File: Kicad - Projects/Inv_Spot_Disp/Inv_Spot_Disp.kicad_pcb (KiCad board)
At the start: 2 copper layers, 137.8 x 68.7 mm, 44 parts, among them J1 PWM_Out, J2 Power_Supply, J3 Current_Sense, J4 Prog, SW1 1, SW2 2, SW3 3, SW4 4, SW5 SW_Push, U1 STM32F030F4Px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

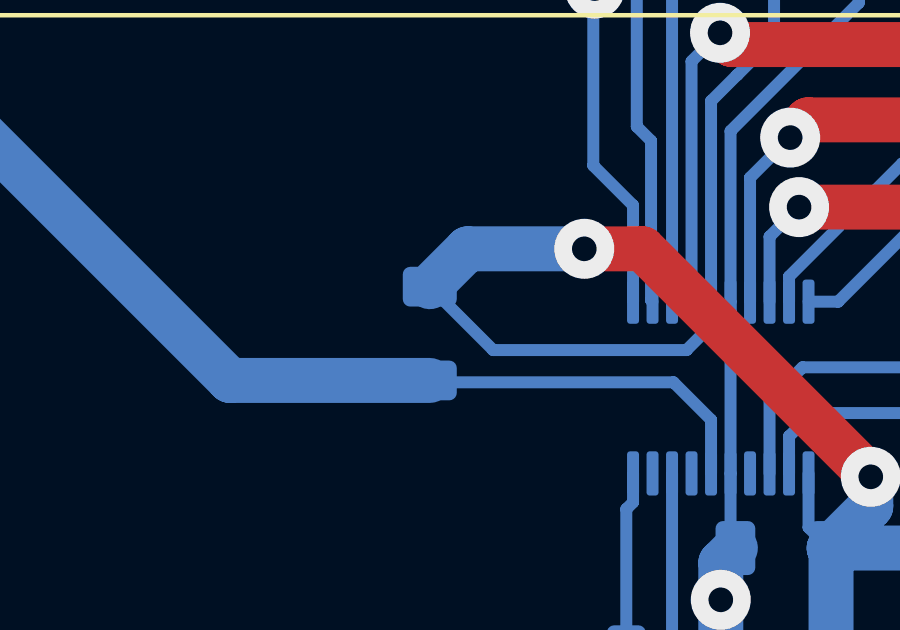
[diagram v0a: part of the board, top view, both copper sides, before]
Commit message: Ajustes de Documentação
Ajustada documentação do módulo LCD e corrigido erro de máscara na função HD_Set_Cursor

Ajustada também posição de capacitor de desacoplamento do sinal do sensor da corrente para ser mais próximo do ADC.
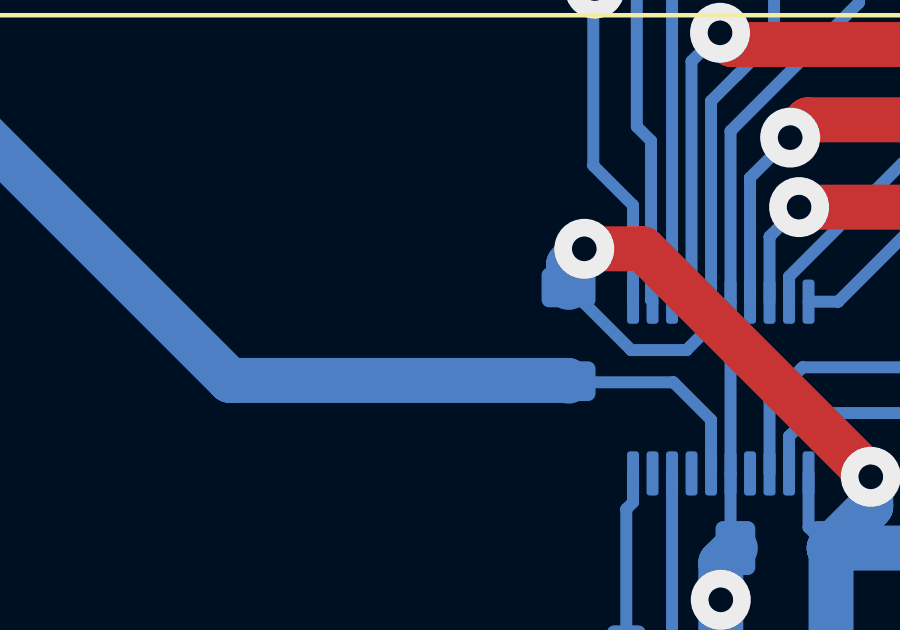
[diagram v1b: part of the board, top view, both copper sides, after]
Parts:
- moved C12 4.63 mm to (91.0, 84.3)
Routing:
- net GND: track 401.3 -> 392.5 mm
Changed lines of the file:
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@@
 	(footprint "Capacitor_SMD:C_1206_3216Metric_Pad1.33x1.80mm_HandSolder"
 		(layer "B.Cu")
-		(at 86.325 84.275 90)
+		(at 90.95 84.3 90)
 		(descr "Capacitor SMD 1206 (3216 Metric), square (rectangular) end terminal, IPC-7351 nominal with elongated pad for handsoldering. (Body size source: IPC-SM-782 page 76, https://www.pcb-3d.com/wordpress/wp-content/uploads/ipc-sm-782a_amendment_1_and_2.pdf)")
 		(tags "capacitor handsolder")
@@
 	)
 	(segment
-		(start 95.7 83.2125)
-		(end 95.7 84.009878)
-		(width 0.4)
-		(layer "B.Cu")
-		(net "GND")
-	)
-	(segment
 		(start 48.3125 76.9425)
 		(end 48.3125 89.8275)
@@
 	)
 	(segment
-		(start 91.475 81.45)
-		(end 87.5875 81.45)
-		(width 1.5)
-		(layer "B.Cu")
-		(net "GND")
-	)
-	(segment
 		(start 92.84 64.98)
 		(end 92.84 62.5)
@@
 	)
 	(segment
-		(start 95.7 84.009878)
-		(end 94.884878 84.825)
+		(start 94.884878 84.825)
+		(end 93.0375 84.825)
 		(width 0.4)
 		(layer "B.Cu")
@@
 	)
 	(segment
+		(start 95.7 83.2125)
+		(end 95.7 84.009878)
+		(width 0.4)
+		(layer "B.Cu")
+		(net "GND")
+	)
+	(segment
+		(start 90.95 81.975)
+		(end 90.95 82.7375)
+		(width 1.5)
+		(layer "B.Cu")
+		(net "GND")
+	)
+	(segment
 		(start 97.8 74.425)
 		(end 97.8 64.05)
@@
 	)
 	(segment
+		(start 95.7 84.009878)
+		(end 94.884878 84.825)
+		(width 0.4)
+		(layer "B.Cu")
+		(net "GND")
+	)
+	(segment
 		(start 128.24 58.64)
 		(end 131.55 61.95)
@@
 	)
 	(segment
-		(start 94.884878 84.825)
-		(end 88.4375 84.825)
-		(width 0.4)
-		(layer "B.Cu")
-		(net "GND")
-	)
-	(segment
 		(start 34.45 87.45)
 		(end 33.525 86.525)
@@
 	)
 	(segment
-		(start 80.192677 58.205177)
-		(end 81.1375 59.15)
+		(start 91.475 81.45)
+		(end 90.95 81.975)
 		(width 1.5)
 		(layer "B.Cu")
@@
 	)
 	(segment
-		(start 48.3125 76.9425)
-		(end 48.3125 83.4625)
+		(start 80.192677 58.205177)
+		(end 81.1375 59.15)
 		(width 1.5)
 		(layer "B.Cu")
@@
 	)
 	(segment
-		(start 87.5875 81.45)
-		(end 86.325 82.7125)
+		(start 48.3125 76.9425)
+		(end 48.3125 83.4625)
 		(width 1.5)
 		(layer "B.Cu")
@@
 	)
 	(segment
+		(start 93.0375 84.825)
+		(end 90.95 82.7375)
+		(width 0.4)
+		(layer "B.Cu")
+		(net "GND")
+	)
+	(segment
 		(start 95.7 76.525)
 		(end 96.575 75.65)
@@
 	)
 	(segment
-		(start 88.4375 84.825)
-		(end 86.325 82.7125)
-		(width 0.4)
-		(layer "B.Cu")
-		(net "GND")
-	)
-	(segment
 		(start 114.435 62.385)
 		(end 114.435 63.885)
@@
 	)
 	(segment
-		(start 94.45 85.9)
-		(end 86.3875 85.9)
+		(start 90.9875 85.9)
+		(end 90.95 85.8625)
 		(width 0.4)
 		(layer "B.Cu")
@@
 	)
 	(segment
-		(start 95.7 88.9375)
-		(end 95.7 87.15)
-		(width 0.4)
+		(start 65.575 71.75)
+		(end 79.6625 85.8375)
+		(width 1.5)
+		(layer "B.Cu")
+		(net "Current_Sense")
+	)
+	(segment
+		(start 79.6625 85.8375)
+		(end 90.925 85.8375)
+		(width 1.5)
 		(layer "B.Cu")
 		(net "Current_Sense")
@@
 	)
 	(segment
-		(start 65.575 71.75)
-		(end 79.6625 85.8375)
-		(width 1.5)
+		(start 95.7 88.9375)
+		(end 95.7 87.15)
+		(width 0.4)
 		(layer "B.Cu")
 		(net "Current_Sense")
 	)
 	(segment
-		(start 79.6625 85.8375)
-		(end 86.325 85.8375)
-		(width 1.5)
+		(start 94.45 85.9)
+		(end 90.9875 85.9)
+		(width 0.4)
 		(layer "B.Cu")
 		(net "Current_Sense")
 	)
 	(segment
-		(start 86.3875 85.9)
-		(end 86.325 85.8375)
-		(width 0.4)
+		(start 90.925 85.8375)
+		(end 90.95 85.8625)
+		(width 1.5)
 		(layer "B.Cu")
 		(net "Current_Sense")

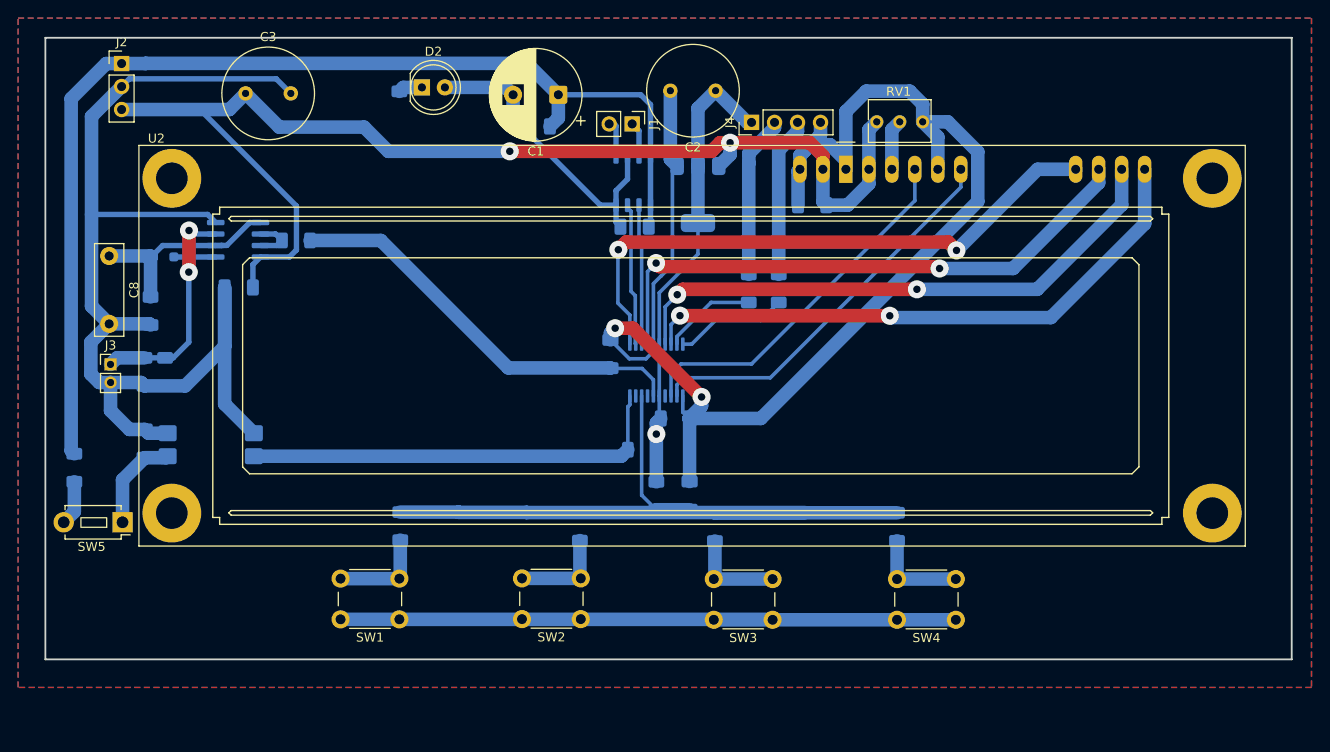
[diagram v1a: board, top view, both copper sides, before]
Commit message: Corrigido Footprint do Display
Corrigido problema com o footprint do display

Melhora o caminho de retorna das trilhas de programação

Aumento na quantidade de vias para reduzir impedância do plano terra
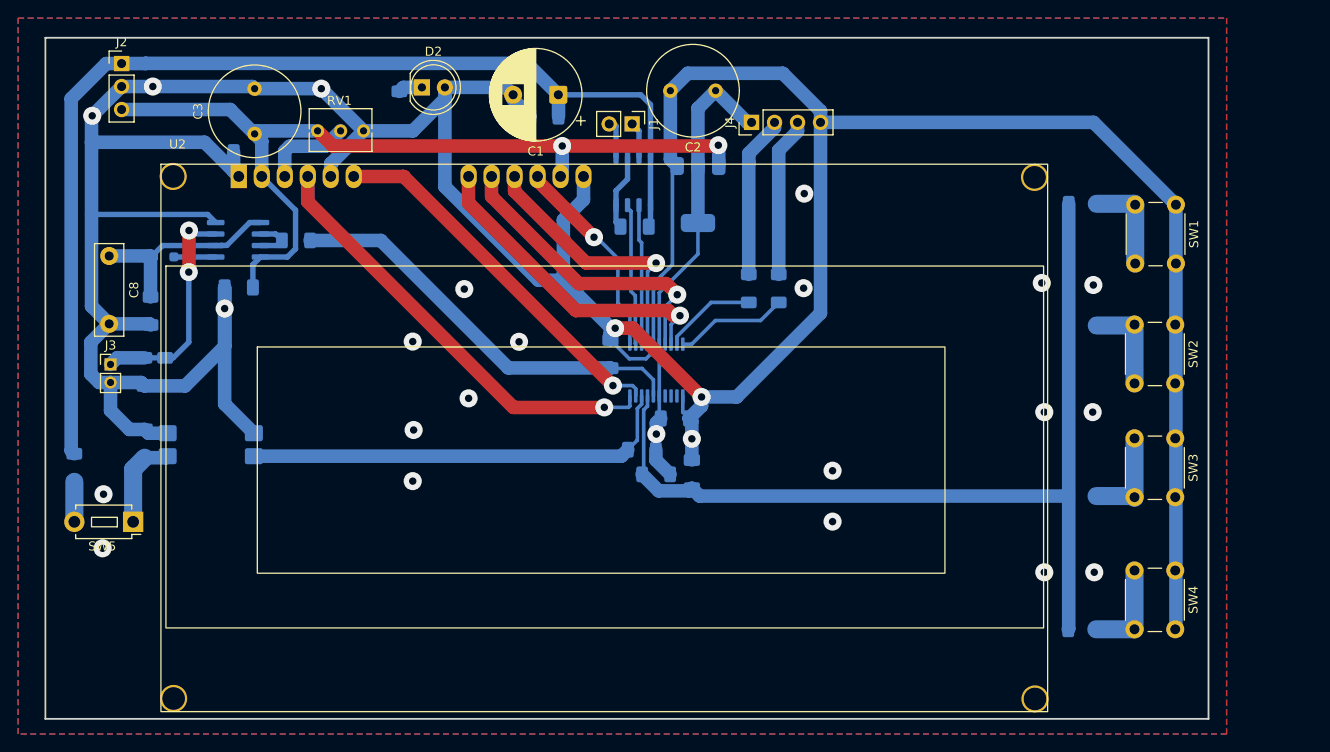
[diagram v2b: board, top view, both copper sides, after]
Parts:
- U2: value LCD-016N002L -> NHD-0420H1Z; footprint Display:LCD-016N002L -> Display:WC1602A
- moved SW1 97.3 mm to (153.4, 67.8), turned to -90 degrees
- moved R2 83.4 mm to (143.2, 67.7), turned to 0 degrees
- moved SW2 73.3 mm to (153.4, 81.0), turned to -90 degrees
- moved U2 67.1 mm to (49.9, 64.7)
- moved C5 62.6 mm to (50.9, 62.0)
- moved RV1 61.8 mm to (58.6, 59.6)
- moved R3 59.9 mm to (143.2, 81.2), turned to 0 degrees
- moved SW3 48.8 mm to (153.4, 93.6), turned to -90 degrees
- moved R4 40.8 mm to (143.1, 100.0), turned to 0 degrees
- moved SW4 24.9 mm to (153.4, 108.2), turned to -90 degrees
- moved R5 23.4 mm to (143.1, 114.7), turned to 0 degrees
- moved C3 4.59 mm to (51.6, 60.0), turned to 90 degrees
- moved C6 2.39 mm to (100.0, 97.6)
- moved R1 2.38 mm to (96.0, 97.6), turned to 180 degrees
- moved C10 1.45 mm to (83.7, 58.0)
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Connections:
- U1 pad 10: Trigger -> RS
- U1 pad 11: D4 -> D7
- U1 pad 14: D5 -> D6
- U1 pad 17: D6 -> D5
- U1 pad 18: D7 -> D4
- U1 pad 2: Enable -> unconnected-(U1-PF0-Pad2)
- U1 pad 3: RS -> unconnected-(U1-PF1-Pad3)
- U1 pad 7: Temp_Sense -> Display_ADC
- U1 pad 8: Display_ADC -> Trigger
- U1 pad 9: unconnected-(U1-PA3-Pad9) -> Enable
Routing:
- net GND: track 392.5 -> 451.2 mm, vias 2 -> 25
- net 5V: track 140.1 -> 96.2 mm
- net D7: track 65.3 -> 22.9 mm, vias 2 -> 1
- net D6: track 63.2 -> 29.9 mm, vias 2 -> 1
- net D4: track 66.0 -> 35.0 mm, vias 2 -> 1
- net D5: track 63.9 -> 33.3 mm, vias 2 -> 1
- net Display_ADC: track 81.9 -> 104.3 mm
- net RS: track 40.8 -> 49.0 mm, vias 0 -> 1
- net Net-(U2-VO): track 5.61 -> 9.90 mm
- net Enable: track 43.6 -> 41.7 mm, vias 0 -> 1
- net 3V3: track 51.5 -> 49.6 mm
- net 15V: track 124.4 -> 122.9 mm
- net Trigger: track 47.7 -> 48.2 mm
- net Net-(C9-Pad1): track 10.8 -> 10.2 mm
- net Net-(R8-Pad1): track 4.96 -> 4.42 mm
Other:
- board size 137.8 x 68.7 mm -> 128.6 x 75.3 mm

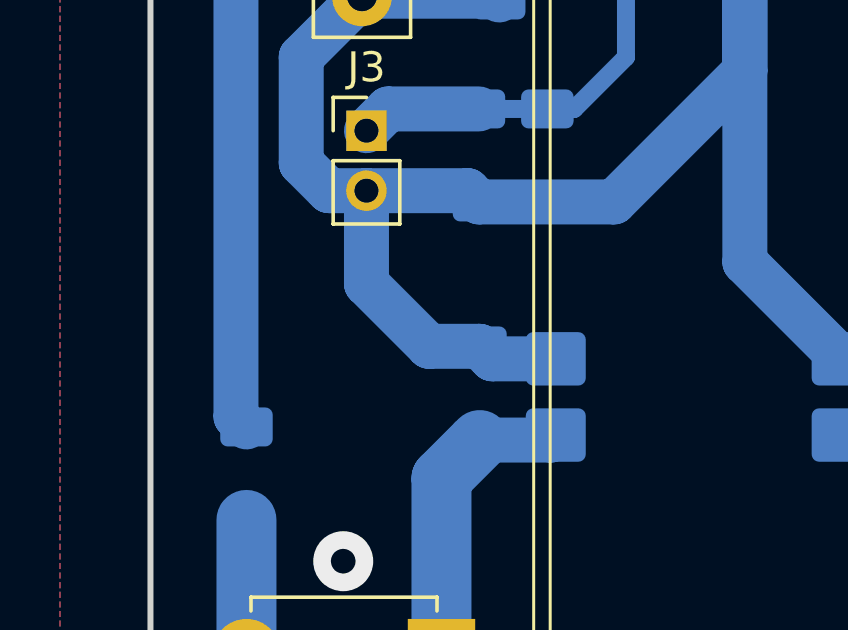
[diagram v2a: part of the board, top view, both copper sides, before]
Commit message: Adição de Vias - Placa de Display
Adicionadas mais algumas vias na placa de display
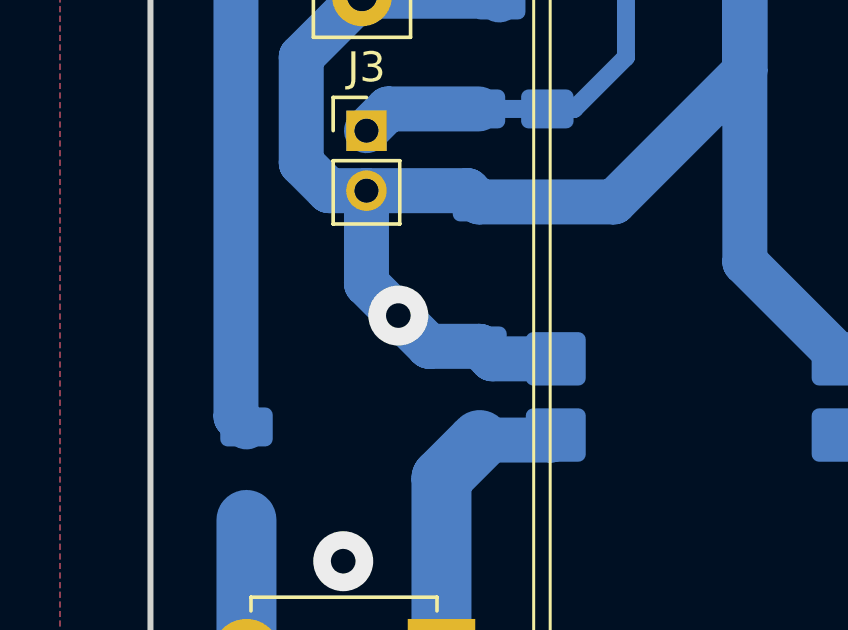
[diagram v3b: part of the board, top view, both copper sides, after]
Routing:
- net GND: vias 25 -> 26
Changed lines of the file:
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@@
+	)
+	(via
+		(at 36.7625 91.6125)
+		(size 2)
+		(drill 0.82)
+		(layers "F.Cu" "B.Cu")
+		(net "GND")
 	)
 	(via
@@
 	)
 	(segment
+		(start 36.7625 91.6125)
+		(end 35.7 90.55)
+		(width 1.5)
+		(layer "B.Cu")
+		(net "GND")
+	)
+	(segment
 		(start 101.025 89.05)
 		(end 101.025 90.0375)
@@
 	(segment
 		(start 37.7875 92.6375)
-		(end 35.7 90.55)
-		(width 1.5)
-		(layer "B.Cu")
+		(end 36.7625 91.6125)
+		(width 1.5)
+		(layer "B.Cu")
